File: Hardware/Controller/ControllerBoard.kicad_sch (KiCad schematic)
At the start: 26 parts, among them J1 Conn_01x08_MountingPin, J2 USB4715-GF-A_REVA, Q1 BC818, Q2 AO3401A, Q3 BC818, X1 CON_JST_PH_2PIN_MTPH2, X2 CON_JST_PH_2PIN_MTPH2

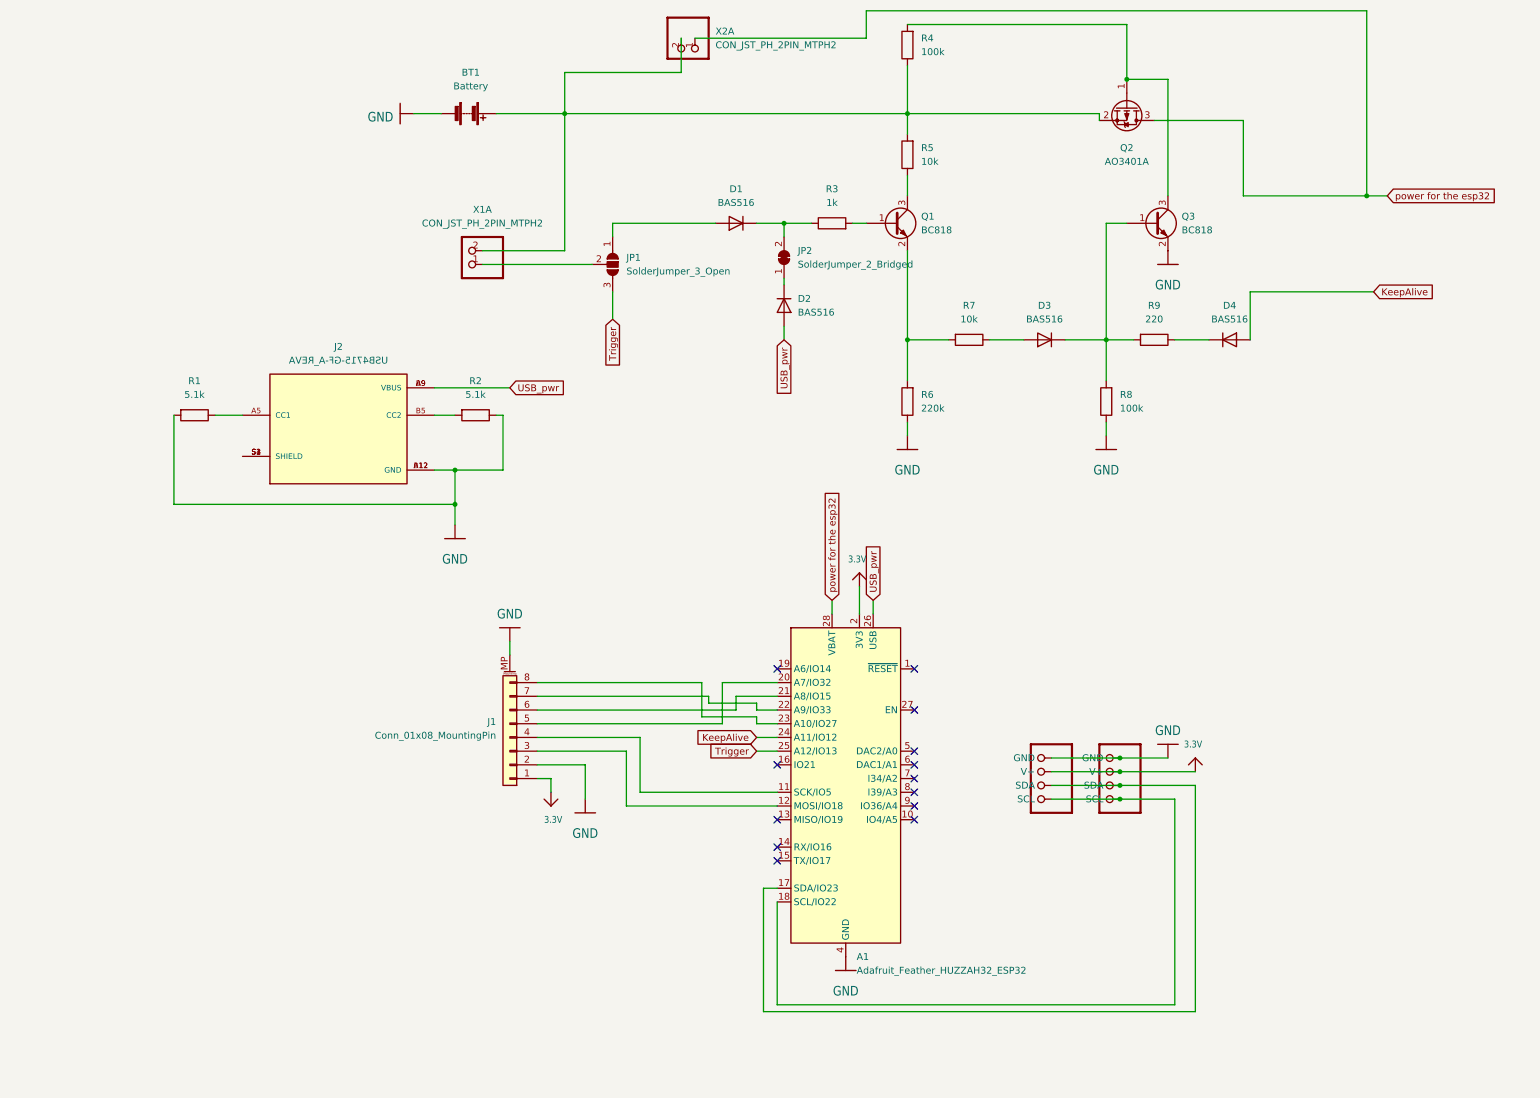
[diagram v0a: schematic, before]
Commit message: Initial conversion and cleanup from a feather to an esp32s3
added USB power
Added switching 3.6-5v regulator
updated schematic ground to use built in kicad libraries
updated partially broken library references to eagle lib files
added circuit simulator of trigger and wakeup simulation

Signed-off-by: lokimetasmith <lokimail@gmail.com>
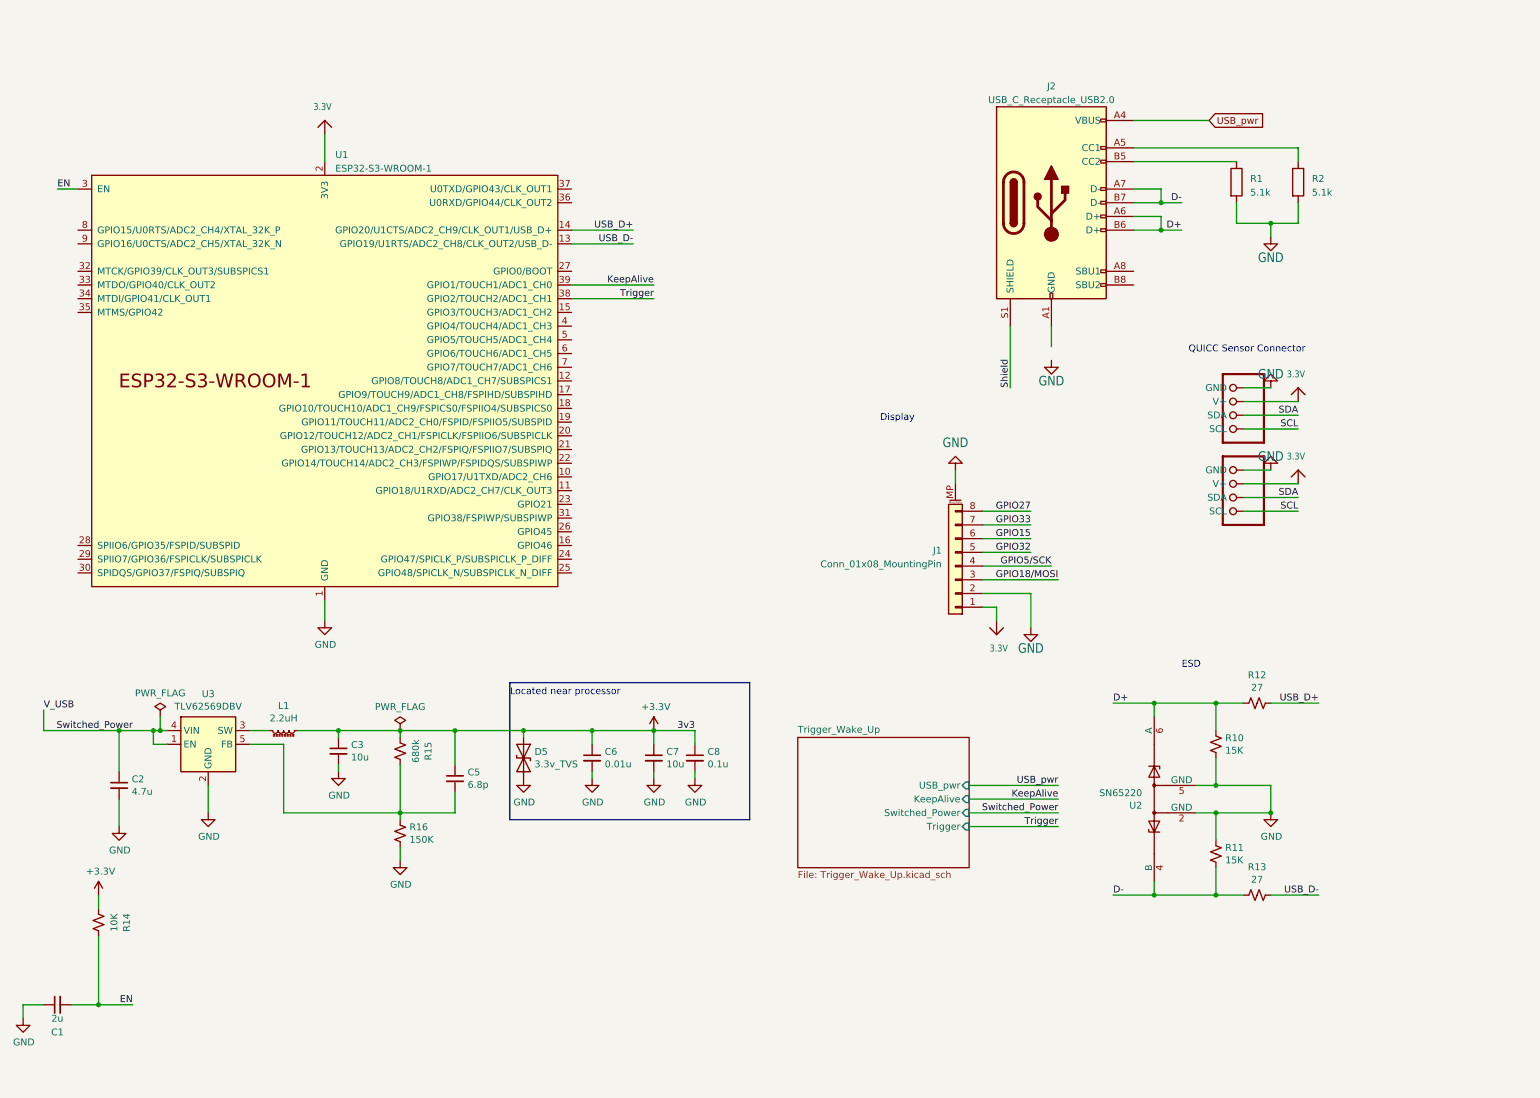
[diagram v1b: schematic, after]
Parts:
- removed A1: Adafruit_Feather_HUZZAH32_ESP32, Module:Adafruit_Feather, symbol MCU_Module:Adafruit_Feather_HUZZAH32_ESP32
- removed BT1: Battery, Battery:BatteryHolder_Keystone_2460_1xAA, symbol Device:Battery
- removed D1, D2, D3, D4: BAS516, Diode_SMD:D_SOD-523, symbol Diode:BAS516
- removed J2: USB4715-GF-A_REVA, USB4715-GF-A_REVA:GCT_USB4715-GF-A_REVA, symbol USB4715-GF-A_REVA:USB4715-GF-A_REVA
- removed JP1: SolderJumper_3_Open, Jumper:SolderJumper-3_P1.3mm_Open_Pad1.0x1.5mm_NumberLabels, symbol Jumper:SolderJumper_3_Open
- removed JP2: SolderJumper_2_Bridged, Jumper:SolderJumper-2_P1.3mm_Bridged_Pad1.0x1.5mm, symbol Jumper:SolderJumper_2_Bridged
- removed Q1, Q3: BC818, Package_TO_SOT_SMD:SOT-23, symbol Transistor_BJT:BC818
- removed Q2: AO3401A, Package_TO_SOT_SMD:SOT-23, symbol Transistor_FET:AO3401A
- removed R3: 1k, Resistor_SMD:R_0603_1608Metric_Pad0.98x0.95mm_HandSolder, symbol Device:R
- removed R4, R8: 100k, Resistor_SMD:R_0603_1608Metric_Pad0.98x0.95mm_HandSolder, symbol Device:R
- removed R5, R7: 10k, Resistor_SMD:R_0603_1608Metric_Pad0.98x0.95mm_HandSolder, symbol Device:R
- removed R6: 220k, Resistor_SMD:R_0603_1608Metric_Pad0.98x0.95mm_HandSolder, symbol Device:R
- removed R9: 220, Resistor_SMD:R_0603_1608Metric_Pad0.98x0.95mm_HandSolder, symbol Device:R
- removed X1, X2: CON_JST_PH_2PIN_MTPH2, Connector_JST:JST_EH_B2B-EH-A_1x02_P2.50mm_Vertical, symbol ControllerBoard-eagle-import:CON_JST_PH_2PIN_MTPH2
- added C1: 2u, Capacitor_SMD:C_0603_1608Metric, symbol temp-sensor-rescue:C_Small-Device-temp-sensor-rescue
- added C2: 4.7u, Capacitor_SMD:C_0805_2012Metric, symbol temp-sensor-rescue:C_Small-Device-temp-sensor-rescue
- added C3, C7: 10u, Capacitor_SMD:C_1206_3216Metric_Pad1.42x1.75mm_HandSolder, symbol temp-sensor-rescue:C_Small-Device-temp-sensor-rescue
- added C5: 6.8p, Capacitor_SMD:C_0402_1005Metric, symbol temp-sensor-rescue:C_Small-Device-temp-sensor-rescue
- added C6: 0.01u, Capacitor_SMD:C_0402_1005Metric, symbol temp-sensor-rescue:C_Small-Device-temp-sensor-rescue
- added C8: 0.1u, Capacitor_SMD:C_0402_1005Metric, symbol temp-sensor-rescue:C_Small-Device-temp-sensor-rescue
- added D5: 3.3v_TVS, Diode_SMD:D_SOD-323, symbol temp-sensor-rescue:D_TVS-Device-temp-sensor-rescue
- added J2: USB_C_Receptacle_USB2.0, Connector_USB:USB_C_Receptacle_GCT_USB4105-xx-A_16P_TopMnt_Horizontal, symbol Connector:USB_C_Receptacle_USB2.0
- added L1: 2.2uH, Inductor_SMD:L_Taiyo-Yuden_MD-4040, symbol Device:L_Core_Ferrite_Small
- added R10, R11: 15K, Resistor_SMD:R_0402_1005Metric, symbol temp-sensor-rescue:R_Small_US-Device-temp-sensor-rescue
- added R12, R13: 27, Resistor_SMD:R_0402_1005Metric, symbol temp-sensor-rescue:R_Small_US-Device-temp-sensor-rescue
- added R14: 10K, Resistor_SMD:R_0402_1005Metric, symbol temp-sensor-rescue:R_Small_US-Device-temp-sensor-rescue
- added R15: 680k, Resistor_SMD:R_0402_1005Metric, symbol temp-sensor-rescue:R_Small_US-Device-temp-sensor-rescue
- added R16: 150K, Resistor_SMD:R_0402_1005Metric, symbol temp-sensor-rescue:R_Small_US-Device-temp-sensor-rescue
- added U1: ESP32-S3-WROOM-1, Espressif:ESP32-S3-WROOM-1, symbol Espressif:ESP32-S3-WROOM-1
- added U2: SN65220, Package_TO_SOT_SMD:SOT-23-6, symbol twig:SN65220-Power_Protection_passthrough
- added U3: TLV62569DBV, Package_TO_SOT_SMD:SOT-23-5, symbol temp-sensor-rescue:TLV62569DBV-Regulator_Switching-temp-sensor-rescue
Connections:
- net 3.3V: now also U1.2 (3V3)
- net GND: now also R2.2, C1.1, C2.2, C3.2, C6.2, C7.2, C8.2, D5.2 (A2), R10.2, R11.1, R16.1, U1.1 (GND), U1.40 (GND), U1.41 (GND), U2.2 (GND), U2.5 (GND), U3.2 (GND); no longer R2.1
- net KeepAlive: now also U1.39 (GPIO1/TOUCH1/ADC1_CH0)
- net Trigger: now also U1.38 (GPIO2/TOUCH2/ADC1_CH1)
- net USB_pwr: now also J2.A4 (VBUS), J2.A9 (VBUS), J2.B4 (VBUS), J2.B9 (VBUS)
- net at R1.1: now also J2.B5 (CC2)
- net GPIO18/MOSI: now reaches J1.3 (Pin_3)
- net GPIO5/SCK: now reaches J1.4 (Pin_4)
- net GPIO32: now reaches J1.5 (Pin_5)
- net GPIO15: now reaches J1.6 (Pin_6)
- net GPIO33: now reaches J1.7 (Pin_7)
- net GPIO27: now reaches J1.8 (Pin_8)
- net SDA: now reaches CONN1.3 (SDA), CONN2.3 (SDA)
- net SCL: now reaches CONN1.4 (SCL), CONN2.4 (SCL)
- new net: L1.1, U3.3 (SW)
- new net: J2.A5 (CC1), R2.1
- new net: C5.2, R15.1, R16.2, U3.5 (FB)
- new net: J2.A1 (GND), J2.A12 (GND), J2.B1 (GND), J2.B12 (GND)
- new net +3V3: C3.1, C5.1, C6.1, C7.1, C8.1, D5.1 (A1), L1.2, R14.2, R15.2
- new net D+: J2.A6 (D+), J2.B6 (D+), R10.1, R12.1, U2.1, U2.6 (A)
- new net D-: J2.A7 (D-), J2.B7 (D-), R11.2, R13.1, U2.3, U2.4 (B)
- new net EN: C1.2, R14.1, U1.3 (EN)
- new net Shield: J2.S1 (SHIELD)
- new net Switched_Power: C2.1, U3.1 (EN), U3.4 (VIN)
- new net USB_D+: R12.2, U1.14 (GPIO20/U1CTS/ADC2_CH9/CLK_OUT1/USB_D+)
- new net USB_D-: R13.2, U1.13 (GPIO19/U1RTS/ADC2_CH8/CLK_OUT2/USB_D-)
- no-connect marks 13 -> 0
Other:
- added sheet Trigger_Wake_Up (Trigger_Wake_Up.kicad_sch)
- note added: "Display"
- note added: "ESD"
- note added: "Located near processor"
- note added: "QUICC Sensor Connector"
- moved on the sheet: J1, R1, R2

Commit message: added footprint for MTSM2601SMF1-100
Signed-off-by: lokimetasmith <lokimail@gmail.com>
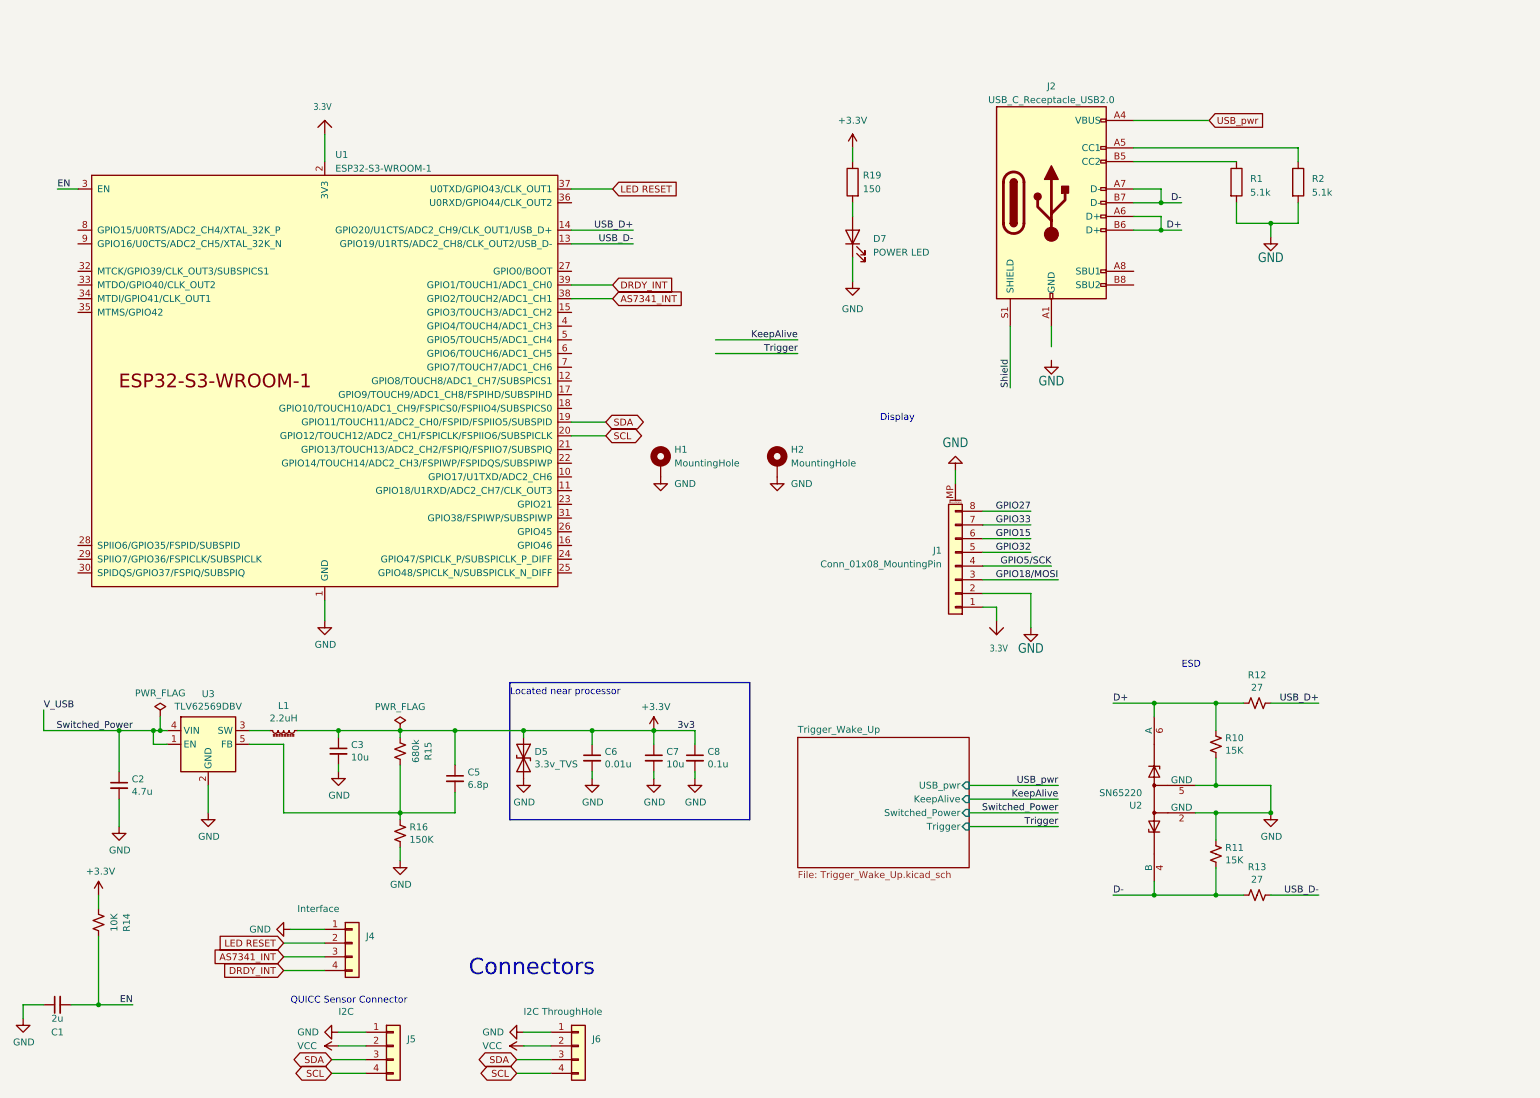
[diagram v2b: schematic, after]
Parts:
- removed CONN1, CONN2: STEMMA_I2C_QT, Connector_JST:JST_SH_SM04B-SRSS-TB_1x04-1MP_P1.00mm_Horizontal, symbol ControllerBoard-eagle-import:STEMMA_I2C_QT
- added D7: POWER LED, LED_SMD:LED_0805_2012Metric_Pad1.15x1.40mm_HandSolder, symbol Device:LED
- added H1, H2: MountingHole, MountingHole:MountingHole_2.2mm_M2_ISO7380_Pad, symbol Mechanical:MountingHole_Pad
- added J4: Interface, Connector_PinSocket_2.54mm:PinSocket_1x04_P2.54mm_Vertical, symbol Connector_Generic:Conn_01x04
- added J5: I2C, Connector_JST:JST_SH_SM04B-SRSS-TB_1x04-1MP_P1.00mm_Horizontal, symbol Connector_Generic:Conn_01x04
- added J6: I2C ThroughHole, Connector_PinSocket_2.54mm:PinSocket_1x04_P2.54mm_Vertical, symbol Connector_Generic:Conn_01x04
- added R19: 150, Resistor_SMD:R_0402_1005Metric, symbol Device:R
- R1, R2: footprint Resistor_SMD:R_0603_1608Metric_Pad0.98x0.95mm_HandSolder -> Resistor_SMD:R_0402_1005Metric
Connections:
- net +3V3: now also R19.1
- net GND: now also D7.1 (K), H1.1, H2.1, J4.1 (Pin_1), J5.1 (Pin_1), J6.1 (Pin_1)
- net KeepAlive: no longer U1.39 (GPIO1/TOUCH1/ADC1_CH0)
- net SCL: now also U1.20 (GPIO12/TOUCH12/ADC2_CH1/FSPICLK/FSPIIO6/SUBSPICLK), J5.4 (Pin_4), J6.4 (Pin_4)
- net SDA: now also U1.19 (GPIO11/TOUCH11/ADC2_CH0/FSPID/FSPIIO5/SUBSPID), J5.3 (Pin_3), J6.3 (Pin_3)
- net Trigger: no longer U1.38 (GPIO2/TOUCH2/ADC1_CH1)
- net LED RESET: now reaches U1.37 (U0TXD/GPIO43/CLK_OUT1)
- net LED RESET: now also J4.2 (Pin_2)
- new net: D7.2 (A), R19.2
- new net AS7341_INT: J4.3 (Pin_3), U1.38 (GPIO2/TOUCH2/ADC1_CH1)
- new net DRDY_INT: J4.4 (Pin_4), U1.39 (GPIO1/TOUCH1/ADC1_CH0)
- new net VCC: J5.2 (Pin_2), J6.2 (Pin_2)
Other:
- note added: "Connectors"

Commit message: second pass on controller rework
Signed-off-by: lokimetasmith <lokimail@gmail.com>
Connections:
- net GND: now also J2.A1 (GND), J2.A12 (GND), J2.B1 (GND), J2.B12 (GND)
- net KeepAlive: now also U1.23 (GPIO21)
- net Trigger: now also U1.26 (GPIO45)
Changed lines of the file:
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@@
   (junction (at 228.6 129.54) (diameter 0) (color 0 0 0 0)
   )
+  (junction (at 77.47 134.62) (diameter 0) (color 0 0 0 0)
+  )
   (junction (at 44.45 134.62) (diameter 0) (color 0 0 0 0)
   )
@@
   (junction (at 88.9 134.62) (diameter 0) (color 0 0 0 0)
   )
-  (junction (at 77.47 134.62) (diameter 0) (color 0 0 0 0)
-  )
   (junction (at 229.87 41.91) (diameter 0) (color 0 0 0 0)
   )
@@
     (stroke (width 0) (type default))
   )
-  (wire (pts (xy 147.32 62.23) (xy 162.56 62.23))
+  (wire (pts (xy 120.65 92.71) (xy 135.89 92.71))
     (stroke (width 0) (type default))
   )
@@
     (stroke (width 0) (type default))
   )
-  (wire (pts (xy 147.32 64.77) (xy 162.56 64.77))
+  (wire (pts (xy 120.65 97.79) (xy 135.89 97.79))
     (stroke (width 0) (type default))
   )
@@
     (stroke (width 0) (type default))
   )
+  (wire (pts (xy 77.47 134.62) (xy 88.9 134.62))
+    (stroke (width 0) (type default))
+  )
   (wire (pts (xy 88.9 149.86) (xy 88.9 151.13))
     (stroke (width 0) (type default))
@@
     (stroke (width 0) (type default))
   )
-  (wire (pts (xy 77.47 134.62) (xy 88.9 134.62))
-    (stroke (width 0) (type default))
-  )
   (polyline (pts (xy 109.22 125.73) (xy 153.67 125.73))
     (stroke (width 0) (type default))
@@
     (stroke (width 0) (type default))
   )
-  (wire (pts (xy 77.47 135.89) (xy 77.47 134.62))
-    (stroke (width 0) (type default))
-  )
   (wire (pts (xy 77.47 140.97) (xy 77.47 142.24))
     (stroke (width 0) (type default))
@@
   )
   (wire (pts (xy 250.19 40.64) (xy 250.19 43.18))
+    (stroke (width 0) (type default))
+  )
+  (wire (pts (xy 77.47 134.62) (xy 77.47 135.89))
     (stroke (width 0) (type default))
   )
@@
     )
   )
-  (label "KeepAlive" (at 162.56 62.23 180) (fields_autoplaced)
+  (label "KeepAlive" (at 135.89 92.71 180) (fields_autoplaced)
     (effects (font (size 1.27 1.27)) (justify right bottom))
-    (property "Intersheetrefs" "${INTERSHEET_REFS}" (at 152.7074 62.23 0)
+    (property "Intersheetrefs" "${INTERSHEET_REFS}" (at 126.0374 92.71 0)
       (effects (font (size 1.27 1.27)) (justify right) hide)
     )
@@
     )
   )
-  (label "Trigger" (at 162.56 64.77 180) (fields_autoplaced)
+  (label "Trigger" (at 135.89 97.79 180) (fields_autoplaced)
     (effects (font (size 1.27 1.27)) (justify right bottom))
-    (property "Intersheetrefs" "${INTERSHEET_REFS}" (at 155.187 64.77 0)
+    (property "Intersheetrefs" "${INTERSHEET_REFS}" (at 128.517 97.79 0)
       (effects (font (size 1.27 1.27)) (justify right) hide)
     )
@@
     )
   )
-  (symbol (lib_id "power:GND") (at 209.55 66.04 0) (unit 1)
+  (symbol (lib_id "power:GND") (at 209.55 63.5 0) (unit 1)
     (in_bom yes) (on_board yes) (dnp no) (fields_autoplaced)
-    (property "Reference" "#GND0103" (at 209.55 66.04 0)
-      (effects (font (size 1.27 1.27)) hide)
-    )
-    (property "Value" "GND" (at 209.55 69.85 0)
+    (property "Reference" "#GND0103" (at 209.55 63.5 0)
+      (effects (font (size 1.27 1.27)) hide)
+    )
+    (property "Value" "GND" (at 209.55 67.31 0)
       (effects (font (size 1.778 1.5113)))
     )
-    (property "Footprint" "ControllerBoard:" (at 209.55 66.04 0)
-      (effects (font (size 1.27 1.27)) hide)
-    )
-    (property "Datasheet" "" (at 209.55 66.04 0)
-      (effects (font (size 1.27 1.27)) hide)
-    )
+    (property "Footprint" "ControllerBoard:" (at 209.55 63.5 0)
+      (effects (font (size 1.27 1.27)) hide)
+    )
+    (property "Datasheet" "" (at 209.55 63.5 0)
+      (effects (font (size 1.27 1.27)) hide)
+    )
